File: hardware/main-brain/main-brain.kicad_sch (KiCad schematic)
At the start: 31 parts, among them J1 19V, J2 CAN+5V, J3 19V OUT, J4 I2S OUT, Q1 AO3481, Q2 2N7000, U1 SN65HVD230

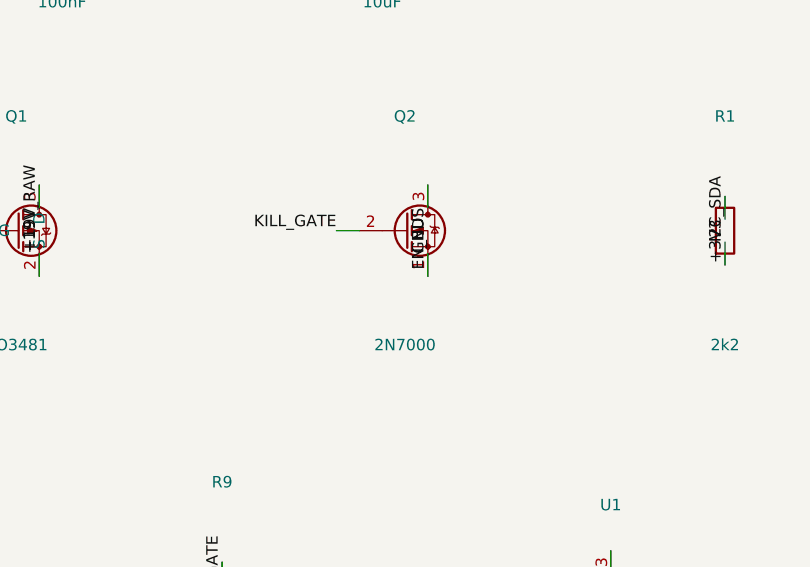
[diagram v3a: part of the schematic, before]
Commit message: Use an AO3400A in SOT-23 for the kill line
The kill-line FET was specified as a 2N7000 in TO-92, which is not a part on
hand. The AO3400A is: single N-channel, SOT-23, Vgs(th) 0.7 V so it is fully
enhanced by a 3.3 V GPIO, and 30 mOhm where the job asks for roughly 120 mA of
sink. KiCad carries the symbol natively with the SOT-23 G/S/D pinout, and it is
the same family, package and pinout as the AO3401A already used for the
reverse-polarity FET.

A dual N-channel in SC-88/SOT-363 was the alternative and works electrically -
Vgs(th) 1.2 V max, 250 mA, 1 Ohm - but it puts a 0.65 mm pitch six-pin part on a
board meant to be hand-soldered and leaves half a device needing its gate tied
off. The single in SOT-23 is the better fit for the same job.

Co-Authored-By: Claude Opus 5 <noreply@anthropic.com>
Claude-Session: https://claude.ai/code/session_011qFNDvbo1RnNn3sy9mr9bh
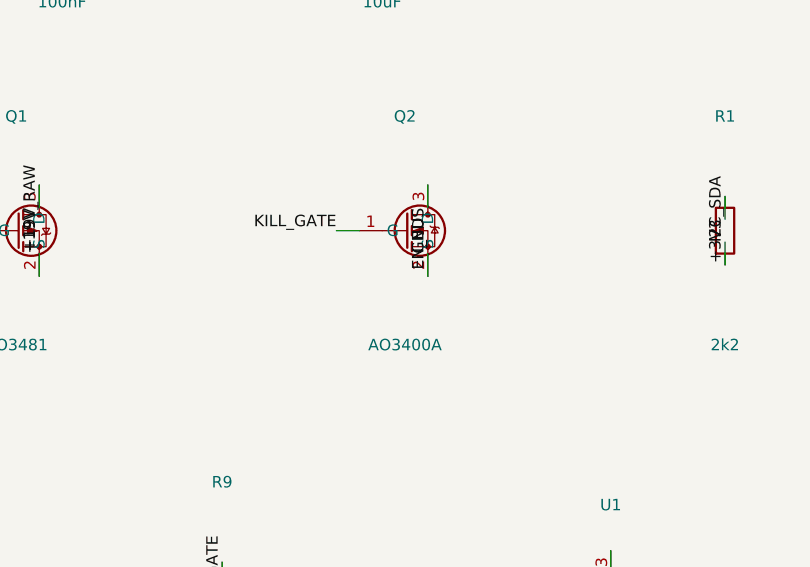
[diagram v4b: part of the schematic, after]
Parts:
- Q2: value 2N7000 -> AO3400A; footprint Package_TO_SOT_THT:TO-92_Inline -> Package_TO_SOT_SMD:SOT-23; symbol Transistor_FET:2N7000 -> Transistor_FET:AO3400A
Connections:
- net GND: now also Q2.2 (S); no longer Q2.1 (S)
- net KILL_GATE: now also Q2.1 (G); no longer Q2.2 (G)
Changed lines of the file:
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@@
 	(wire
 		(pts
-			(xy 241.3 144.78) (xy 241.3 142.24)
+			(xy 233.68 139.7) (xy 231.14 139.7)
 		)
 		(stroke
@@
 	(wire
 		(pts
-			(xy 233.68 139.7) (xy 231.14 139.7)
+			(xy 241.3 144.78) (xy 241.3 142.24)
 		)
 		(stroke
@@
 		)
 	)
-	(label "GND"
-		(at 241.3 142.24 90)
+	(label "KILL_GATE"
+		(at 231.14 139.7 180)
 		(effects
 			(font
 				(size 1.27 1.27)
 			)
-			(justify left bottom)
+			(justify right bottom)
 		)
 	)
-	(label "KILL_GATE"
-		(at 231.14 139.7 180)
+	(label "GND"
+		(at 241.3 142.24 90)
 		(effects
 			(font
 				(size 1.27 1.27)
 			)
-			(justify right bottom)
+			(justify left bottom)
 		)
 	)
@@
 	)
 	(symbol
-		(lib_id "Transistor_FET:2N7000")
+		(lib_id "Transistor_FET:AO3400A")
 		(at 238.76 139.7 0)
 		(unit 1)
@@
 			)
 		)
-		(property "Value" "2N7000"
+		(property "Value" "AO3400A"
 			(at 238.76 152.4 0)
 			(effects
@@
 			)
 		)
-		(property "Footprint" "Package_TO_SOT_THT:TO-92_Inline"
+		(property "Footprint" "Package_TO_SOT_SMD:SOT-23"
 			(at 238.76 139.7 0)
 			(effects
@@
 		(on_board yes)
 		(dnp no)
-		(property "Reference" "#PWR104"
+		(property "Reference" "#PWR374"
 			(at 30 206.9 0)
 			(effects
@@
 			(project "main-brain"
 				(path "/0f59cd00-4aec-49c6-a79a-ca571be7adeb"
-					(reference "#PWR104")
+					(reference "#PWR374")
 					(unit 1)
 				)
@@
 		(on_board yes)
 		(dnp no)
-		(property "Reference" "#FLG104"
+		(property "Reference" "#FLG374"
 			(at 42.7 206.9 0)
 			(effects
@@
 			(project "main-brain"
 				(path "/0f59cd00-4aec-49c6-a79a-ca571be7adeb"
-					(reference "#FLG104")
+					(reference "#FLG374")
 					(unit 1)
 				)
@@
 		(on_board yes)
 		(dnp no)
-		(property "Reference" "#PWR571"
+		(property "Reference" "#PWR710"
 			(at 68.1 206.9 0)
 			(effects
@@
 			(project "main-brain"
 				(path "/0f59cd00-4aec-49c6-a79a-ca571be7adeb"
-					(reference "#PWR571")
+					(reference "#PWR710")
 					(unit 1)
 				)
@@
 		(on_board yes)
 		(dnp no)
-		(property "Reference" "#FLG571"
+		(property "Reference" "#FLG710"
 			(at 80.8 206.9 0)
 			(effects
@@
 			(project "main-brain"
 				(path "/0f59cd00-4aec-49c6-a79a-ca571be7adeb"
-					(reference "#FLG571")
+					(reference "#FLG710")
 					(unit 1)
 				)
@@
 		(on_board yes)
 		(dnp no)
-		(property "Reference" "#PWR438"
+		(property "Reference" "#PWR119"
 			(at 106.2 206.9 0)
 			(effects
@@
 			(project "main-brain"
 				(path "/0f59cd00-4aec-49c6-a79a-ca571be7adeb"
-					(reference "#PWR438")
+					(reference "#PWR119")
 					(unit 1)
 				)
@@
 		(on_board yes)
 		(dnp no)
-		(property "Reference" "#FLG438"
+		(property "Reference" "#FLG119"
 			(at 118.9 206.9 0)
 			(effects
@@
 			(project "main-brain"
 				(path "/0f59cd00-4aec-49c6-a79a-ca571be7adeb"
-					(reference "#FLG438")
+					(reference "#FLG119")
 					(unit 1)
 				)
@@
 		(on_board yes)
 		(dnp no)
-		(property "Reference" "#PWR193"
+		(property "Reference" "#PWR858"
 			(at 144.3 206.9 0)
 			(effects
@@
 			(project "main-brain"
 				(path "/0f59cd00-4aec-49c6-a79a-ca571be7adeb"
-					(reference "#PWR193")
+					(reference "#PWR858")
 					(unit 1)
 				)
@@
 		(on_board yes)
 		(dnp no)
-		(property "Reference" "#FLG193"
+		(property "Reference" "#FLG858"
 			(at 157 206.9 0)
 			(effects
@@
 			(project "main-brain"
 				(path "/0f59cd00-4aec-49c6-a79a-ca571be7adeb"
-					(reference "#FLG193")
+					(reference "#FLG858")
 					(unit 1)
 				)
@@
 		(on_board yes)
 		(dnp no)
-		(property "Reference" "#PWR288"
+		(property "Reference" "#PWR472"
 			(at 182.4 206.9 0)
 			(effects
@@
 			(project "main-brain"
 				(path "/0f59cd00-4aec-49c6-a79a-ca571be7adeb"
-					(reference "#PWR288")
+					(reference "#PWR472")
 					(unit 1)
 				)
@@
 		(on_board yes)
 		(dnp no)
-		(property "Reference" "#FLG288"
+		(property "Reference" "#FLG472"
 			(at 195.1 206.9 0)
 			(effects
@@
 			(project "main-brain"
 				(path "/0f59cd00-4aec-49c6-a79a-ca571be7adeb"
-					(reference "#FLG288")
+					(reference "#FLG472")
 					(unit 1)
 				)

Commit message: Lay the node out around right-angle connectors, and spec what it can do
The connector order is all right-angle JST: 3-pin XH, 5-pin XH and 2-pin VH,
with no 2-pin XH at all. A right-angle body opens toward +Y at 0 degrees, so
the rotation is what points a cable off the board, and the placer had no
concept of rotation - it put J2 through the crystal and pushed J1 and J7 past
the outline.

kigen.rotate_boxes turns a footprint's courtyard with it; pinned entries now
take an optional third element; check.py rotates the library courtyard before
testing overlap and outline, and verifies the angle as well as the position.

Floorplan, following the three placement rules:
  - CAN on opposite edges, J2 left and J3 right
  - the whole motor loom on the bottom edge: phases, NTC, encoder, SPI
  - power and SWD on the top
All eight ports are on the perimeter, none closer than 1.1 mm to an edge.

Four things the auto-placer got wrong and are now pinned:
  - U6 sat under the driver module, stacking the LDO's heat under the bridge's
  - R7 sat on A1's exact origin; it belongs under the module, but deliberately
    placed clear of every pad rather than by accident
  - both crystal load caps sat at one end of a 20 mm hand-solder footprint,
    leaving one of them 22 mm from its terminal
  - the node-ID pull-ups were stranded 13 mm from their jumpers

Vbus divider R4 4k7 -> 10k. 100 k / 4k7 read 19 V as 0.85 V, a quarter of the
ADC span. 100 k / 10 k reads 1.73 V and clips at 36 V.

Two renderer bugs, both only visible once something was rotated or mirrored:
  - pad angles were being summed with the footprint angle, but KiCad stores a
    pad's angle absolutely
  - the mirror reflected about the origin rather than the view box, and the
    substrate rect took its min in board space instead of screen space, so the
    bottom view sat 13 mm left and grew a slab off the far edge

New docs:
  - docs/capabilities.md - bus range, torque and current resolution, loop
    rates, CAN bandwidth a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
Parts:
- J2: footprint Connector_JST:JST_XH_B5B-XH-AM_1x05_P2.50mm_Vertical -> Connector_JST:JST_XH_S5B-XH-A_1x05_P2.50mm_Horizontal
- J3: footprint Connector_JST:JST_VH_B2P-VH_1x02_P3.96mm_Vertical -> Connector_JST:JST_VH_S2P-VH_1x02_P3.96mm_Horizontal
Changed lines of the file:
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@@
 			)
 		)
-		(property "Footprint" "Connector_JST:JST_XH_B5B-XH-AM_1x05_P2.50mm_Vertical"
+		(property "Footprint" "Connector_JST:JST_XH_S5B-XH-A_1x05_P2.50mm_Horizontal"
 			(at 53.34 139.7 0)
 			(effects
@@
 			)
 		)
-		(property "Footprint" "Connector_JST:JST_VH_B2P-VH_1x02_P3.96mm_Vertical"
+		(property "Footprint" "Connector_JST:JST_VH_S2P-VH_1x02_P3.96mm_Horizontal"
 			(at 86.36 134.62 0)
 			(effects
@@
 		(on_board yes)
 		(dnp no)
-		(property "Reference" "#PWR779"
+		(property "Reference" "#PWR620"
 			(at 30 206.9 0)
 			(effects
@@
 			(project "main-brain"
 				(path "/0f59cd00-4aec-49c6-a79a-ca571be7adeb"
-					(reference "#PWR779")
+					(reference "#PWR620")
 					(unit 1)
 				)
@@
 		(on_board yes)
 		(dnp no)
-		(property "Reference" "#FLG779"
+		(property "Reference" "#FLG620"
 			(at 42.7 206.9 0)
 			(effects
@@
 			(project "main-brain"
 				(path "/0f59cd00-4aec-49c6-a79a-ca571be7adeb"
-					(reference "#FLG779")
+					(reference "#FLG620")
 					(unit 1)
 				)
@@
 		(on_board yes)
 		(dnp no)
-		(property "Reference" "#PWR419"
+		(property "Reference" "#PWR541"
 			(at 68.1 206.9 0)
 			(effects
@@
 			(project "main-brain"
 				(path "/0f59cd00-4aec-49c6-a79a-ca571be7adeb"
-					(reference "#PWR419")
+					(reference "#PWR541")
 					(unit 1)
 				)
@@
 		(on_board yes)
 		(dnp no)
-		(property "Reference" "#FLG419"
+		(property "Reference" "#FLG541"
 			(at 80.8 206.9 0)
 			(effects
@@
 			(project "main-brain"
 				(path "/0f59cd00-4aec-49c6-a79a-ca571be7adeb"
-					(reference "#FLG419")
+					(reference "#FLG541")
 					(unit 1)
 				)
@@
 		(on_board yes)
 		(dnp no)
-		(property "Reference" "#PWR138"
+		(property "Reference" "#PWR687"
 			(at 106.2 206.9 0)
 			(effects
@@
 			(project "main-brain"
 				(path "/0f59cd00-4aec-49c6-a79a-ca571be7adeb"
-					(reference "#PWR138")
+					(reference "#PWR687")
 					(unit 1)
 				)
@@
 		(on_board yes)
 		(dnp no)
-		(property "Reference" "#FLG138"
+		(property "Reference" "#FLG687"
 			(at 118.9 206.9 0)
 			(effects
@@
 			(project "main-brain"
 				(path "/0f59cd00-4aec-49c6-a79a-ca571be7adeb"
-					(reference "#FLG138")
+					(reference "#FLG687")
 					(unit 1)
 				)
@@
 		(on_board yes)
 		(dnp no)
-		(property "Reference" "#PWR816"
+		(property "Reference" "#PWR397"
 			(at 144.3 206.9 0)
 			(effects
@@
 			(project "main-brain"
 				(path "/0f59cd00-4aec-49c6-a79a-ca571be7adeb"
-					(reference "#PWR816")
+					(reference "#PWR397")
 					(unit 1)
 				)
@@
 		(on_board yes)
 		(dnp no)
-		(property "Reference" "#FLG816"
+		(property "Reference" "#FLG397"
 			(at 157 206.9 0)
 			(effects
@@
 			(project "main-brain"
 				(path "/0f59cd00-4aec-49c6-a79a-ca571be7adeb"
-					(reference "#FLG816")
+					(reference "#FLG397")
 					(unit 1)
 				)
@@
 		(on_board yes)
 		(dnp no)
-		(property "Reference" "#PWR409"
+		(property "Reference" "#PWR291"
 			(at 182.4 206.9 0)
 			(effects
@@
 			(project "main-brain"
 				(path "/0f59cd00-4aec-49c6-a79a-ca571be7adeb"
-					(reference "#PWR409")
+					(reference "#PWR291")
 					(unit 1)
 				)
@@
 		(on_board yes)
 		(dnp no)
-		(property "Reference" "#FLG409"
+		(property "Reference" "#FLG291"
 			(at 195.1 206.9 0)
 			(effects
@@
 			(project "main-brain"
 				(path "/0f59cd00-4aec-49c6-a79a-ca571be7adeb"
-					(reference "#FLG409")
-					(unit 1)
-				)
+					(reference "#FLG291")
+					(unit 1)
+				)
